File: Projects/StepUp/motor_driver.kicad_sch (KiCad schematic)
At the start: 1 part, among them U1 TMC2300-LA

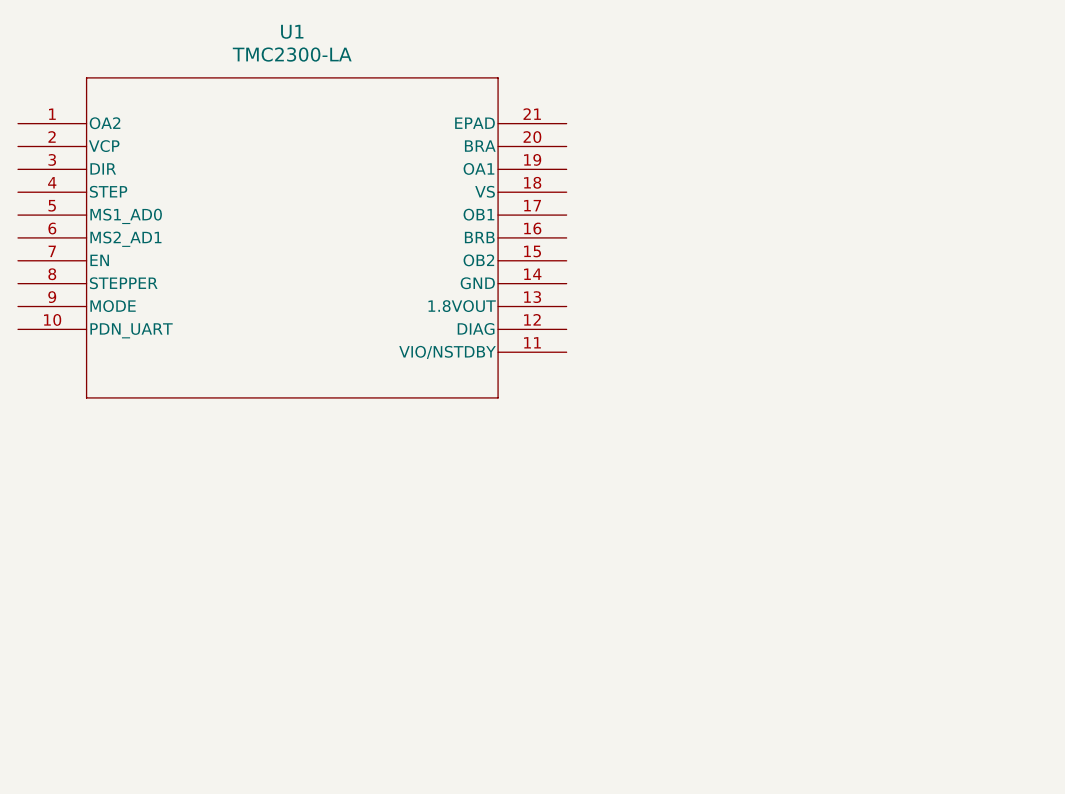
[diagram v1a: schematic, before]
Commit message: feat(rp2040): Layout begins, extra libraries
RPico minimal project downloaded + assets copied. Boost converter layout
in progress, 18650 battery holder added.
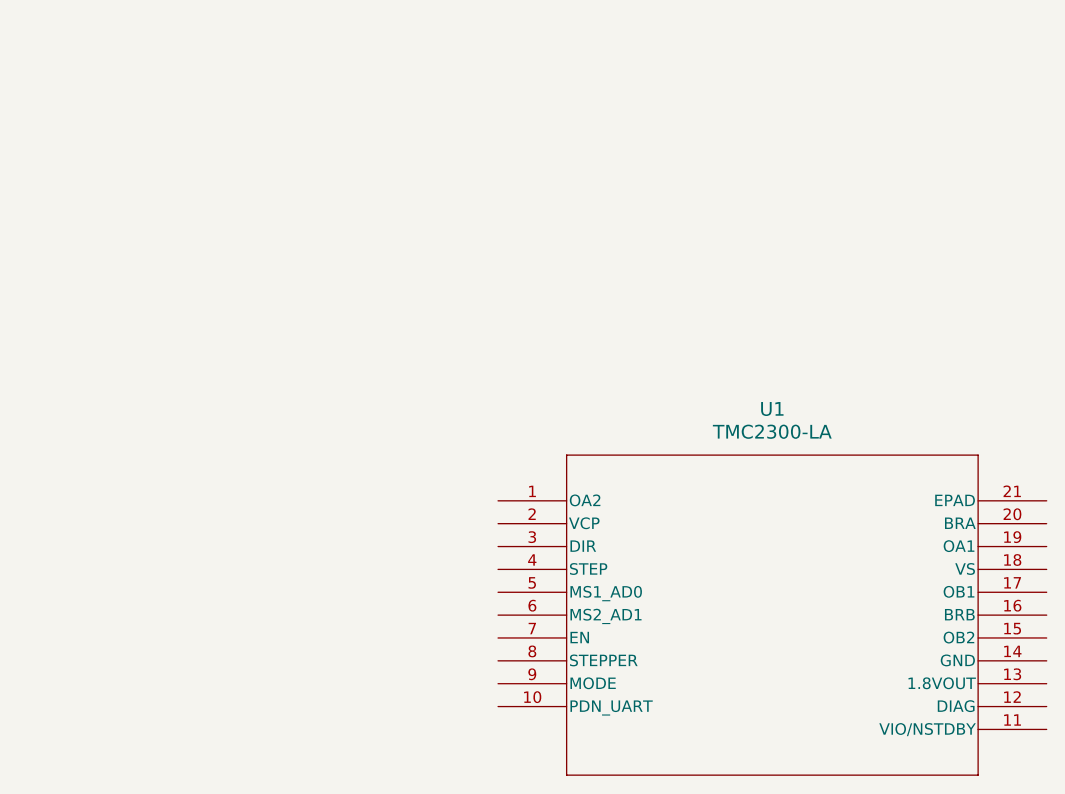
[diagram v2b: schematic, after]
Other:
- moved on the sheet: U1
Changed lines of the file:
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@@
 	(generator "eeschema")
 	(generator_version "8.0")
-	(paper "A4")
+	(paper "A3")
 	(title_block
 		(title "Motor Driver")
@@
 	(symbol
 		(lib_id "2024-01-13_14-51-57:TMC2300-LA")
-		(at 116.84 91.44 0)
+		(at 170.18 133.35 0)
 		(unit 1)
 		(exclude_from_sim no)
@@
 		(fields_autoplaced yes)
 		(property "Reference" "U1"
-			(at 147.32 81.28 0)
+			(at 200.66 123.19 0)
 			(effects
 				(font
@@
 		)
 		(property "Value" "TMC2300-LA"
-			(at 147.32 83.82 0)
+			(at 200.66 125.73 0)
 			(effects
 				(font
@@
 		)
 		(property "Footprint" "footprints:QFN20_3x3_TRI-L"
-			(at 116.84 91.44 0)
+			(at 170.18 133.35 0)
 			(effects
 				(font
@@
 		)
 		(property "Datasheet" "TMC2300-LA"
-			(at 116.84 91.44 0)
+			(at 170.18 133.35 0)
 			(effects
 				(font
@@
 		)
 		(property "Description" ""
-			(at 116.84 91.44 0)
+			(at 170.18 133.35 0)
 			(effects
 				(font

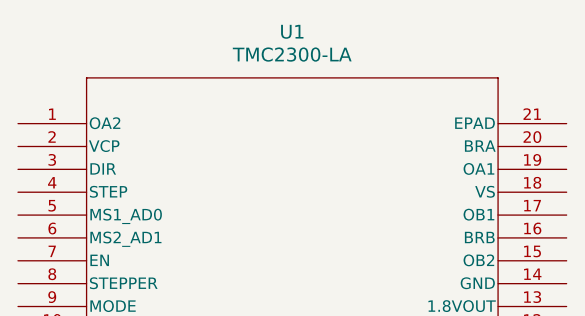
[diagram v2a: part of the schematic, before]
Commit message: feat(power): Input stage updates
USB vs Vbat source selection using PMOS gate logic.
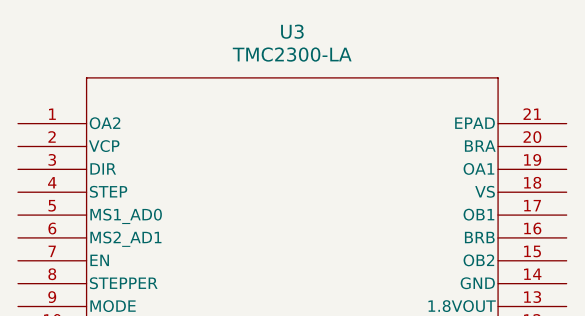
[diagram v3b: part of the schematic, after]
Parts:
- U3: renamed from U1; footprint footprints:QFN20_3x3_TRI-L -> Ultra_librarian_footprints:QFN20_3x3_TRI
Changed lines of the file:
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@@
 		(dnp no)
 		(fields_autoplaced yes)
-		(property "Reference" "U1"
+		(property "Reference" "U3"
 			(at 200.66 123.19 0)
 			(effects
@@
 			)
 		)
-		(property "Footprint" "footprints:QFN20_3x3_TRI-L"
+		(property "Footprint" "Ultra_librarian_footprints:QFN20_3x3_TRI"
 			(at 170.18 133.35 0)
 			(effects
@@
 			(project "StepUp"
 				(path "/e0cca1c7-c263-49eb-8c40-74000ebe5285/f5cf6bff-0c76-4311-a1f3-856e1fd3b2e7"
-					(reference "U1")
+					(reference "U3")
 					(unit 1)
 				)

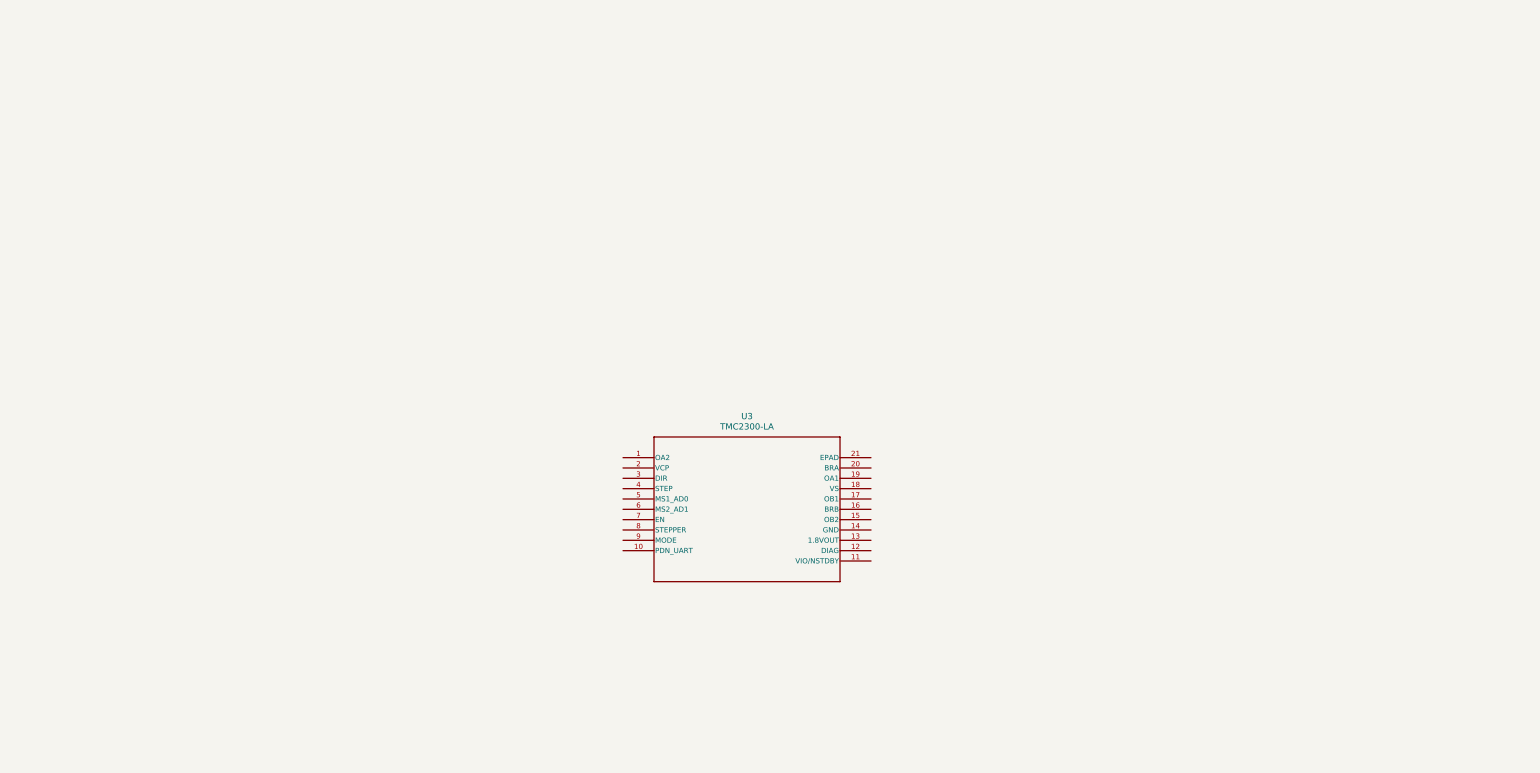
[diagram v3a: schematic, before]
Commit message: feat(stepup): Schematic + PCB updates
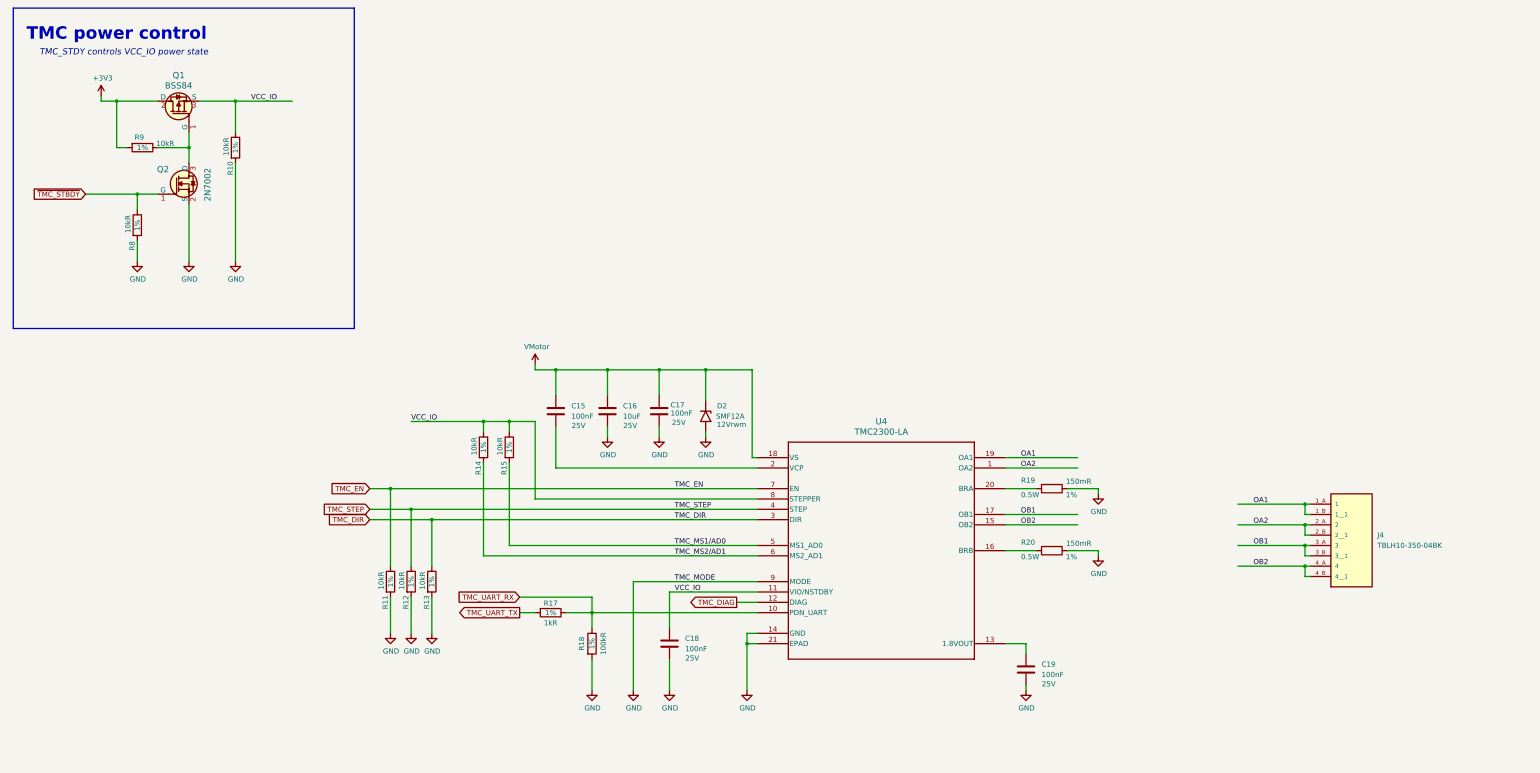
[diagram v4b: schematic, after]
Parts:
- added C15, C17, C18, C19: 100nF, Capacitor_SMD:C_0603_1608Metric, symbol Device:C
- added C16: 10uF, Capacitor_SMD:C_0805_2012Metric, symbol Device:C
- added D2: SMF12A, Diode_SMD:D_SMF, symbol Diode:SMF12A
- added J4: TBLH10-350-04BK, Snapeda:CUI_TBLH10-350-04BK, symbol Snapeda:TBLH10-350-04BK
- added Q1: BSS84, digikey-footprints:SOT-23-3, symbol dk_Transistors-FETs-MOSFETs-Single:BSS84
- added Q2: 2N7002, digikey-footprints:SOT-23-3, symbol dk_Transistors-FETs-MOSFETs-Single:2N7002
- added R10, R11, R12, R13, R14, R15, R8, R9: 10kR, Resistor_SMD:R_0603_1608Metric, symbol Device:R
- added R17: 1kR, Resistor_SMD:R_0603_1608Metric, symbol Device:R
- added R18: 100kR, Resistor_SMD:R_0603_1608Metric, symbol Device:R
- added R19, R20: 150mR, Resistor_SMD:R_1206_3216Metric, symbol Device:R
- U4: renamed from U3; footprint Ultra_librarian_footprints:QFN20_3x3_TRI -> QFN20_3x3_TRI
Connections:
- net OA2: now reaches U4.1 (OA2)
- net OA2: now also J4.2_A (2), J4.2_B (2__1)
- net TMC_UART_RX: now reaches U4.10 (PDN_UART)
- net TMC_UART_RX: now also R17.1, R18.1
- net VCC_IO: now reaches U4.11 (VIO/NSTDBY)
- net VCC_IO: now also U4.8 (STEPPER), C18.1, Q1.3 (S), R10.1, R14.1, R15.1
- net TMC_DIAG: now reaches U4.12 (DIAG)
- net at U4.13 (1.8VOUT): now also C19.1
- net GND: now reaches U4.14 (GND)
- net GND: now also U4.21 (EPAD), U4.9 (MODE), C16.2, C17.2, C18.2, C19.2, D2.2 (A2), Q2.2 (S), R10.2, R11.2, R12.2, R13.2, R18.2, R19.1, R20.1, R8.2
- net OB2: now reaches U4.15 (OB2)
- net OB2: now also J4.4_A (4), J4.4_B (4__1)
- net at U4.16 (BRB): now also R20.2
- net OB1: now reaches U4.17 (OB1)
- net OB1: now also J4.3_A (3), J4.3_B (3__1)
- net VMotor: now reaches U4.18 (VS)
- net VMotor: now also C15.1, C16.1, C17.1, D2.1 (A1)
- net OA1: now reaches U4.19 (OA1)
- net OA1: now also J4.1_A (1), J4.1_B (1__1)
- net at U4.2 (VCP): now also C15.2
- net at U4.20 (BRA): now also R19.2
- net TMC_DIR: now reaches U4.3 (DIR)
- net TMC_DIR: now also R13.1
- net TMC_STEP: now reaches U4.4 (STEP)
- net TMC_STEP: now also R12.1
- net TMC_MS1/AD0: now reaches U4.5 (MS1_AD0)
- net TMC_MS1/AD0: now also R15.2
- net TMC_MS2/AD1: now reaches U4.6 (MS2_AD1)
- net TMC_MS2/AD1: now also R14.2
- net TMC_EN: now reaches U4.7 (EN)
- net TMC_EN: now also R11.1
- new net: Q1.1 (G), Q2.3 (D), R9.1
- new net +3V3: Q1.2 (D), R9.2
- new net TMC_UART_TX: R17.2
- new net ~{TMC_STBDY}: Q2.1 (G), R8.1
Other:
- note added: "TMC power control"
- note added: "TMC_STDY controls VCC_IO power state"
- moved on the sheet: U4

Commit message: feat(schematic): Ready for layout
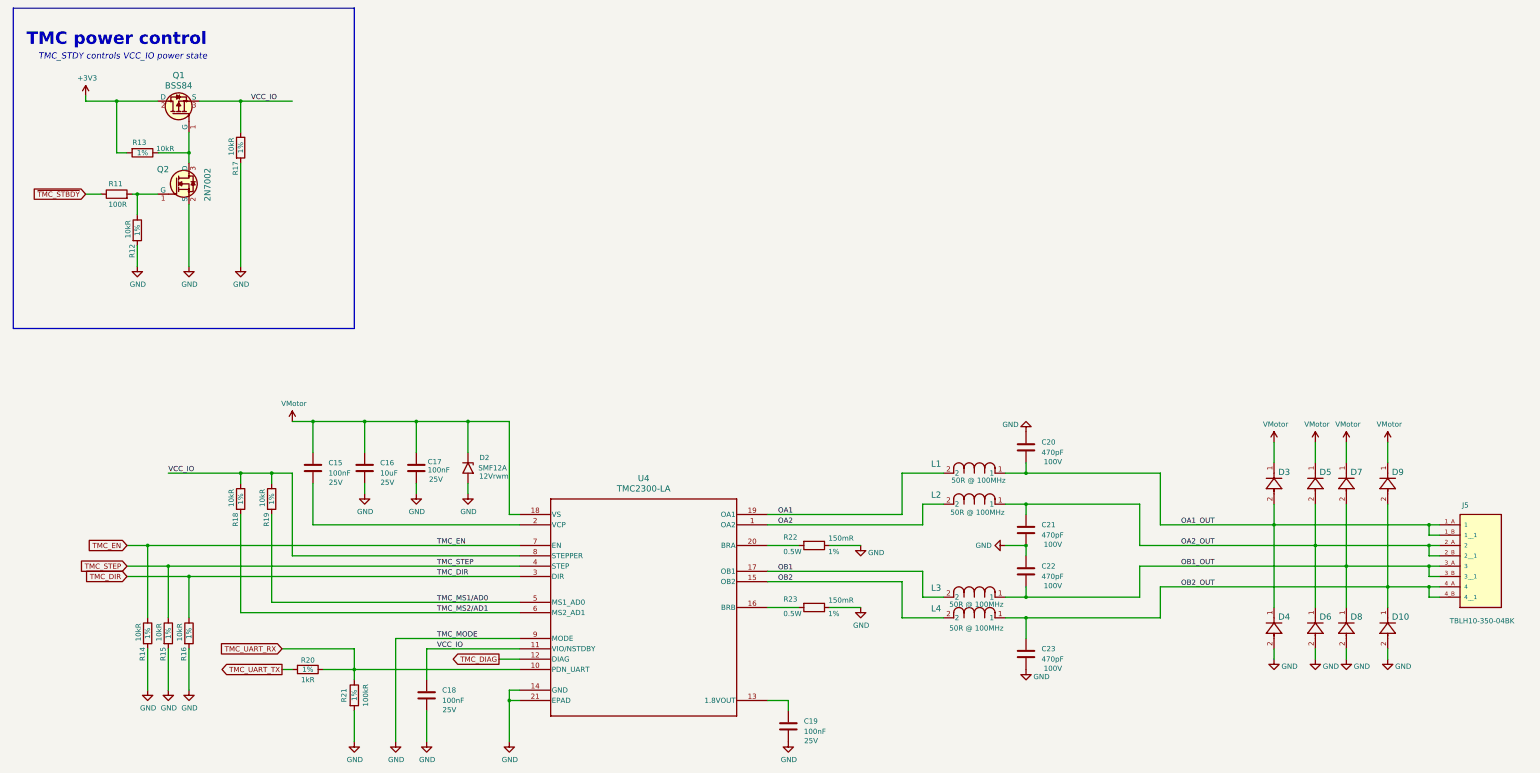
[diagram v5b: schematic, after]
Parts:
- added C20, C21, C22, C23: 470pF, Capacitor_SMD:C_0603_1608Metric, symbol Device:C
- added D10, D3, D4, D5, D6, D7, D8, D9: SSA33L-E3/61T, Snapeda:DIODE_DO214AC, symbol Snapeda_kicad_2:SSA33L-E3_61T
- added L1, L2, L3, L4: HI1206T500R-10, Snapeda:IND_HI1206T500R-10_LRD, symbol Snapeda_kicad_2:HI1206T500R-10
- added R11: 100R, Resistor_SMD:R_0603_1608Metric, symbol Device:R
- renumbered J4 to J5, R8 to R12, R9 to R13, R11 to R14, R12 to R15, R13 to R16, R10 to R17, R14 to R18, R15 to R19, R17 to R20, R18 to R21, R19 to R22, R20 to R23
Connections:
- net GND: now also C20.1, C21.2, C22.1, C23.2, D10.2, D4.2, D6.2, D8.2
- net OA1: now also L1.2; no longer J5.1_A (1), J5.1_B (1__1)
- net OA2: now also L2.2; no longer J5.2_A (2), J5.2_B (2__1)
- net OB1: now also L3.2; no longer J5.3_A (3), J5.3_B (3__1)
- net OB2: now also L4.2; no longer J5.4_A (4), J5.4_B (4__1)
- net VMotor: now also D3.1, D5.1, D7.1, D9.1
- net ~{TMC_STBDY}: now also R11.1; no longer Q2.1 (G), R12.1
- new net: Q2.1 (G), R11.2, R12.1
- new net OA1_OUT: C20.2, D3.2, D4.1, J5.1_A (1), J5.1_B (1__1), L1.1
- new net OA2_OUT: C21.1, D5.2, D6.1, J5.2_A (2), J5.2_B (2__1), L2.1
- new net OB1_OUT: C22.2, D7.2, D8.1, J5.3_A (3), J5.3_B (3__1), L3.1
- new net OB2_OUT: C23.1, D10.1, D9.2, J5.4_A (4), J5.4_B (4__1), L4.1
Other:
- moved on the sheet: C15, C16, C17, C18, C19, D2, J5, R12, R13, R14, R15, R16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
